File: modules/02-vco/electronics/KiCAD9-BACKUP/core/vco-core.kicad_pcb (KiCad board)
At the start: 2 copper layers, 58 x 110 mm, 146 parts, among them J1 Conn_01x04, J2 Conn_02x05_Odd_Even, J3 Conn_02x05_Odd_Even, J4 Conn_01x02, J5 Conn_02x03_Odd_Even, J6 Conn_02x02_Counter_Clockwise, J8 Conn_01x07, Q1 BC847BS, Q2 MMBT3906, Q3 J111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

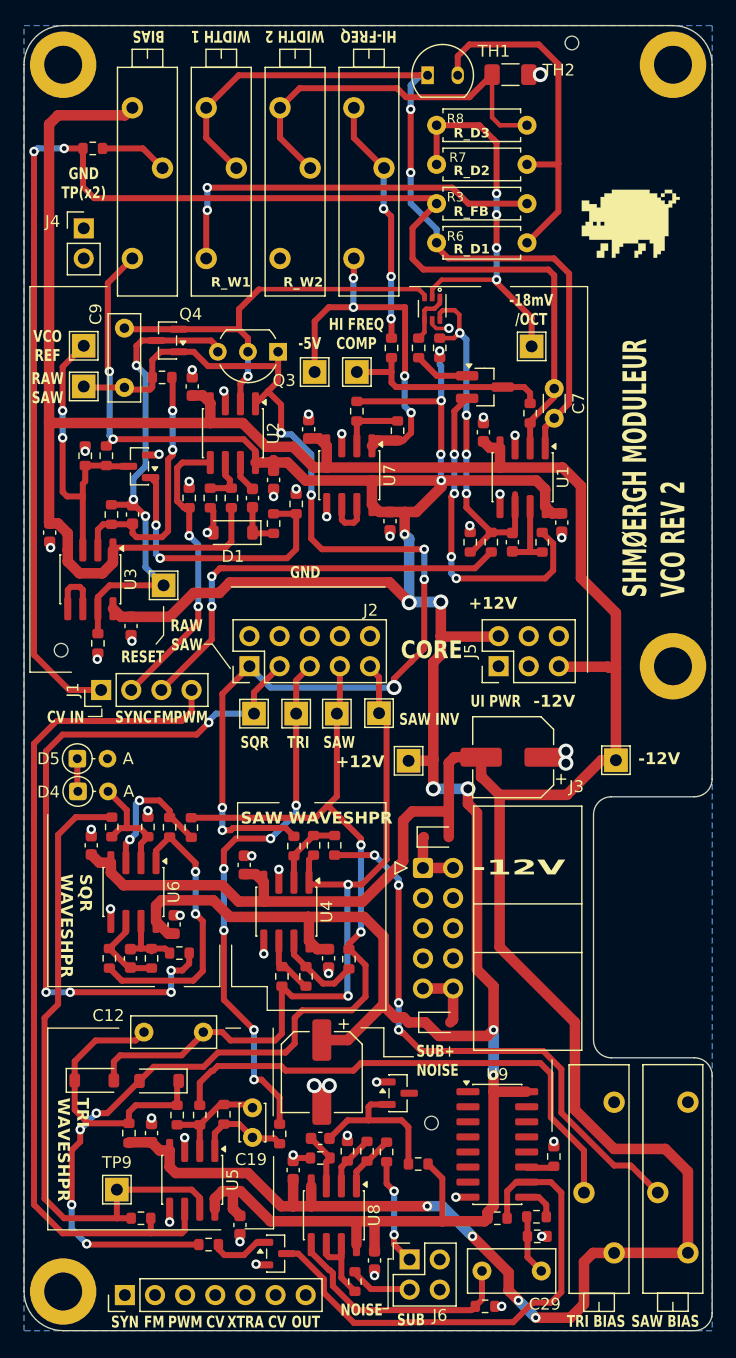
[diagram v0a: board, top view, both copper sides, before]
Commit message: Fix: Replace generic MMBT3906 with ON Semi for Q2
Q2 is the actuator in the master current servo loop (U1B → Q2) that sets the tail current for the exponential converter. The previous BOM specified the generic LCSC part C7420354, which JLCPCB silently substituted between production batches: batch 1 (Jan 2026) received a working part, while batches 2 and 3 received Zhuhai Hongjiacheng (R+O) MMBT3906 parts under the same C-code.

The R+O datasheet only characterizes hFE at IC = −10 mA and above, with no minimum specified at low collector currents. The circuit operates Q2 at sub-milliamp currents, where the substituted part has insufficient gain to close the servo loop. U1B saturates against the negative supply rail trying to compensate, leaving Q2's collector current stuck at a fixed (too-low) value regardless of CV input.
Symptoms across all affected boards (20+ units, fully uniform):

- VCO pitch ceiling at ~70 Hz
- Pitch plateaus and flattens above a certain CV — no further response to increasing CV
- R_BIAS1 trim has no effect on output (loop railed)
- TP1 floats at ~1V instead of being servoed to 0V
- U1B output pinned at −10.3V (TL072 negative rail)

Verified by swapping Q2 with a verified-genuine 2N3906 on two broken boards — both immediately tracked V/oct correctly across full CV range.
The replacement part ON Semi MMBT3906LT1G (LCSC C53444) explicitly specifies hFE ≥ 60 at IC = −0.1 mA in its datasheet, guaranteeing correct behavior in this circuit's operating range.
Changes:

BOM: Q2 LCSC part number changed from C7420354 → C53444
Schematic annotation updated to specify ON Semi MMBT3906LT1G
Production note added: "Q2 (C53444): Do not substitute. Must be ON Semi MMBT3906LT1G."
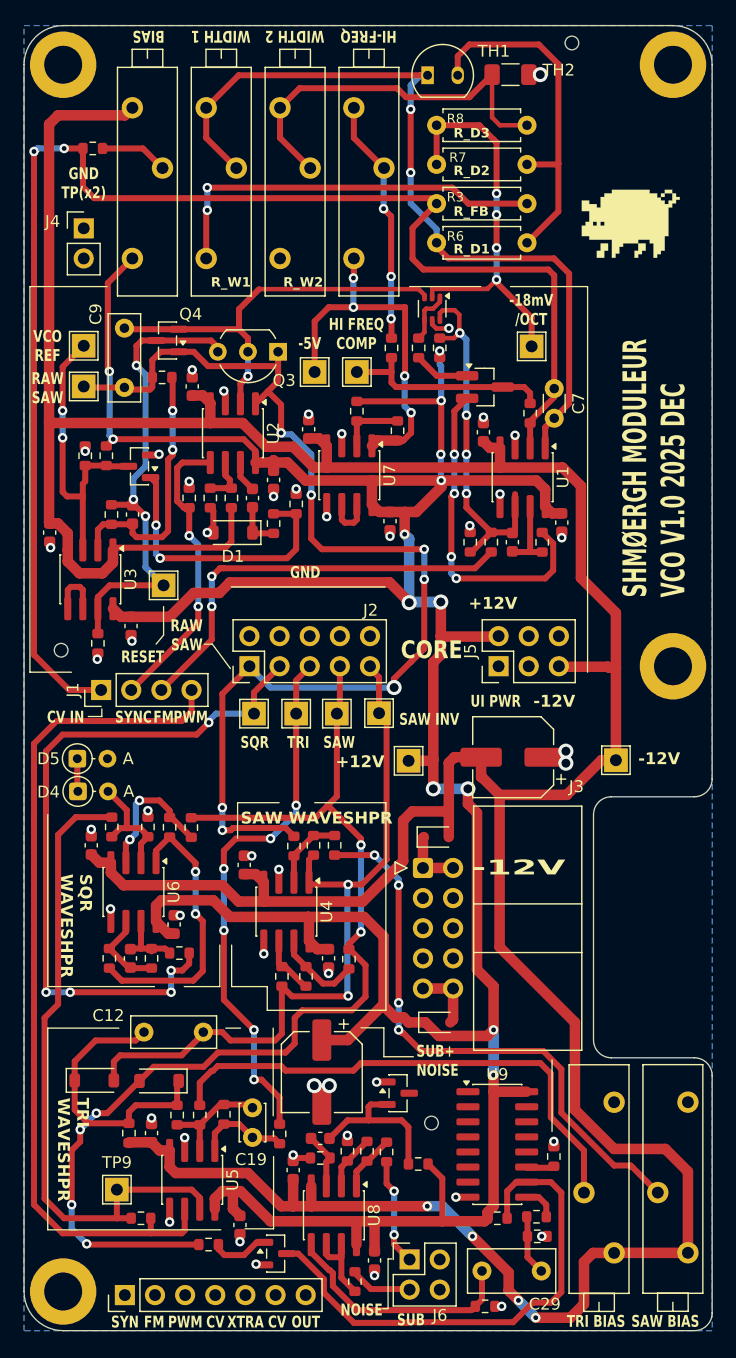
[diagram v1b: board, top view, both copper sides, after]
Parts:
- Q1: footprint Shmoergh_Custom_Footprints:SOT-363_SC-70-6 -> Package_TO_SOT_SMD:SOT-363_SC-70-6
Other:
- board text added: "SHMØERGH MODULEUR VCO V1.0 2025 DEC"
- board text added: "SM-02 Analog VCO Core V1.0 / 2025 Dec"
- board text removed: "SHMØERGH MODULEUR VCO REV 2"
- board text removed: "VCO Core REV 1"
